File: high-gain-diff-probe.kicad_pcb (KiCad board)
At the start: 4 copper layers, 120 x 74.5 mm, 104 parts, among them J1 30V DC IN, J2 BNC, J4 BNC, J5 BNC, SW1 DP3T, SW2 DP3T, SW3 SPDT, SW4 DP3T, SW5 DP3T, SW6 SPDT, SW7 DP3T, U1 AD8428BRZ, U2 OP1177, U3 BUF634A, U6 LM393, U7 AD8671, U8 BUF634A

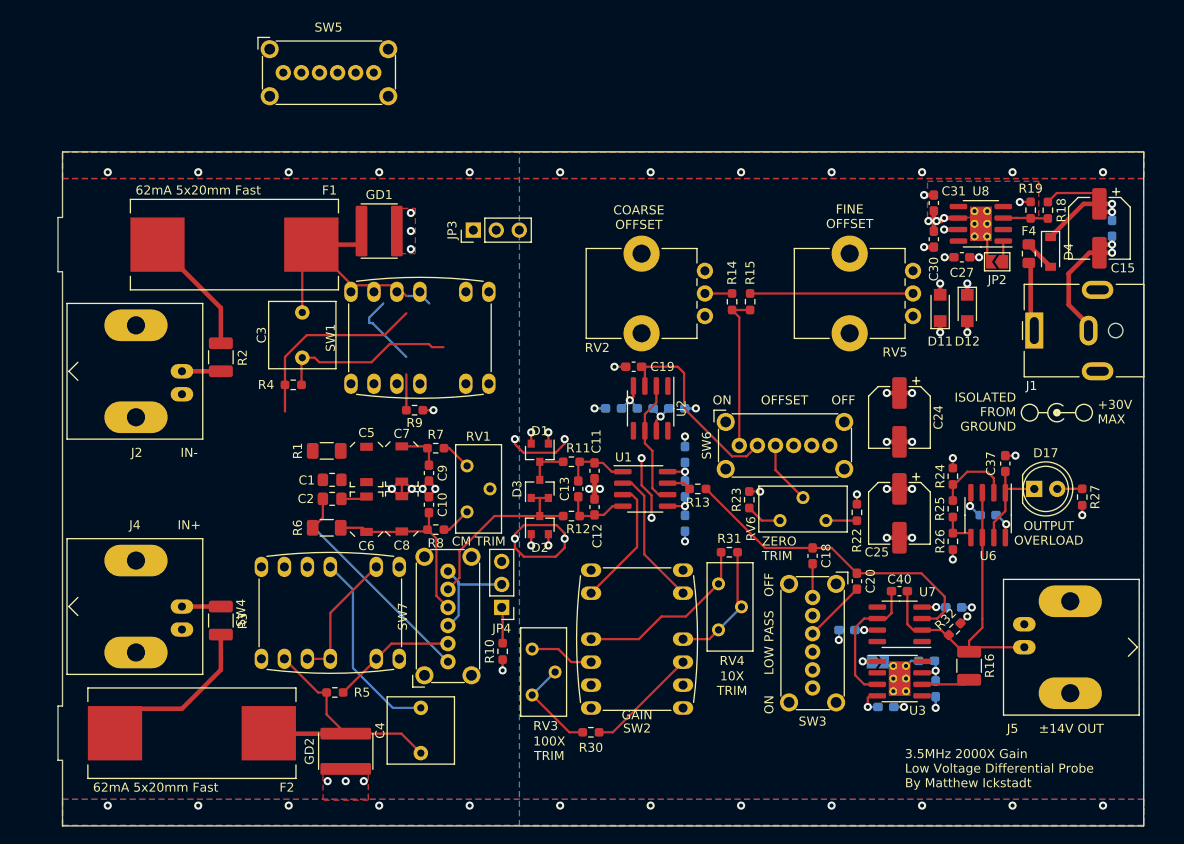
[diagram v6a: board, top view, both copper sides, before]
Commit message: Complete major layout of no-relay design
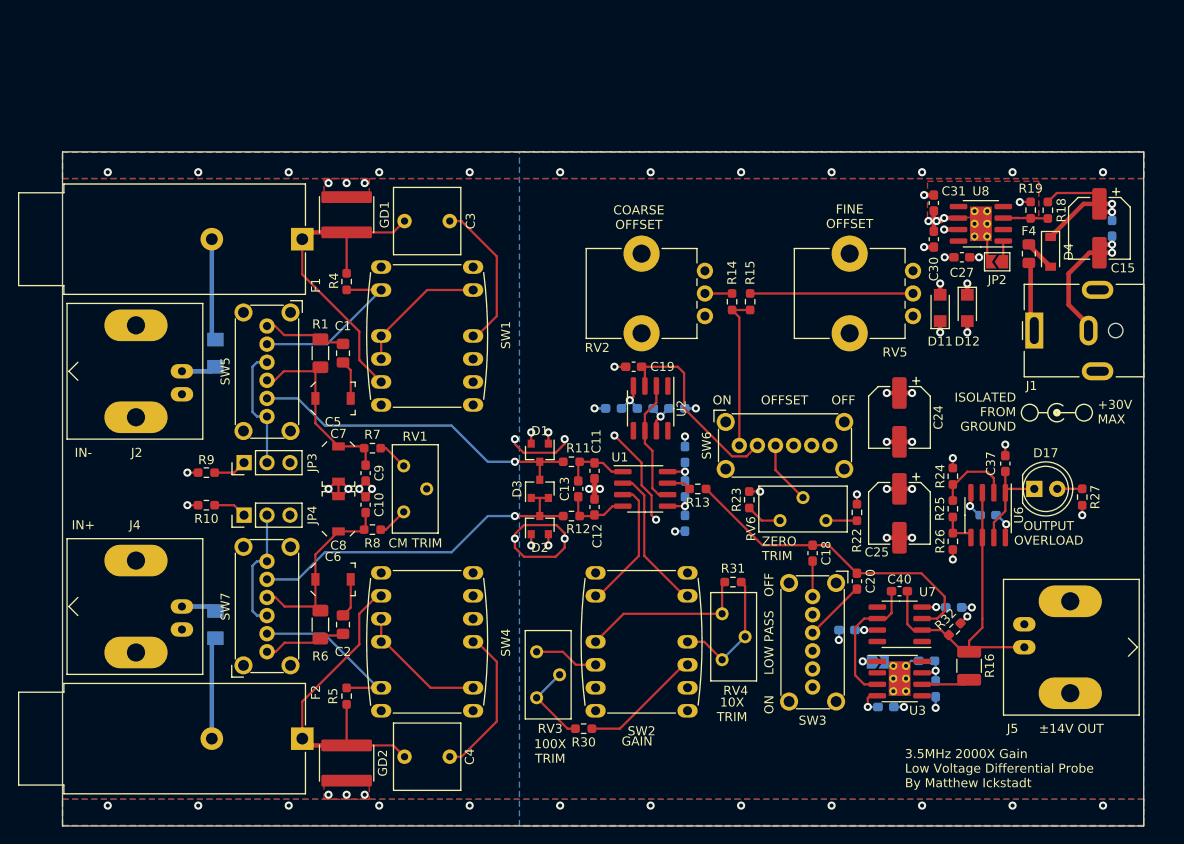
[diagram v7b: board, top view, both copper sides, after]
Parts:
- F1, F2: footprint high-gain-diff-probe:Fuseholder_Schurter_0031.8273 -> Fuse:Fuseholder_Cylinder-5x20mm_Schurter_FAB_0031-355x_Horizontal_Closed
- R2, R3: footprint Resistor_SMD:R_1210_3225Metric_Pad1.30x2.65mm_HandSolder -> Resistor_SMD:R_MiniMELF_MMA-0204; moved to B.Cu
- moved R10 36.5 mm to (105.9, 101.8), turned to 0 degrees
- moved JP3 36.1 mm to (110.1, 97.1)
- moved JP4 30.3 mm to (110.1, 102.9), turned to 90 degrees
- moved SW5 28.1 mm to (112.6, 82.0), turned to 270 degrees
- moved R9 24.0 mm to (105.9, 98.2), turned to 180 degrees
- moved C3 22.2 mm to (132.8, 70.4), turned to 180 degrees
- moved SW7 20.0 mm to (112.6, 118.0)
- moved C1 14.1 mm to (121.0, 85.0), turned to 90 degrees
- moved C2 14.0 mm to (121.0, 115.0), turned to 270 degrees
- moved R4 12.8 mm to (121.4, 77.1), turned to 270 degrees
- moved F2 12.2 mm to (116.5, 127.6)
- moved SW4 11.2 mm to (130.3, 116.9), turned to 270 degrees
- moved R1 10.8 mm to (118.5, 85.0), turned to 90 degrees
- moved R6 10.7 mm to (118.5, 115.0), turned to 270 degrees
- moved C5 8.18 mm to (119.9, 90.0), turned to 0 degrees
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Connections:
- R9 pad 1: Net-(JP3-Pad2) -> Net-(JP3-Pad1)
- SW1 pad 1: (no net) -> Net-(C3-Pad2)
- SW1 pad 2: GND -> Net-(SW1-Pad2)
- SW1 pad 3: Net-(C3-Pad1) -> Net-(SW1-Pad2)
- SW1 pad 4: Net-(C3-Pad2) -> (no net)
- SW1 pad 5: Net-(SW1-Pad5) -> GND
- SW1 pad 6: Net-(SW1-Pad5) -> Net-(C3-Pad1)
- SW1 pad C1: Net-(SW1-Pad5) -> Net-(R4-Pad2)
- SW1 pad C2: Net-(R4-Pad2) -> Net-(SW1-Pad2)
- SW5 pad 3: Net-(JP3-Pad1) -> Net-(JP3-Pad2)
- SW5 pad 6: Net-(JP3-Pad1) -> Net-(JP3-Pad2)
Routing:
- net /ATTEN-: track 4.59 -> 37.6 mm, vias 0 -> 1
- net /ATTEN+: track 21.7 -> 39.5 mm, vias 0 -> 1
- net Net-(C5-Pad1): track 4.86 -> 21.4 mm
- net (no net): track 15.7 -> 0.00 mm, vias 2 -> 0
- net Net-(C2-Pad2): track 24.4 -> 9.22 mm
- net Net-(SW1-Pad2): track 0.00 -> 14.8 mm
- net Net-(JP3-Pad2): track 3.98 -> 13.7 mm
- net Net-(C3-Pad2): track 26.3 -> 36.0 mm
- net GND: track 98.8 -> 89.5 mm, vias 61 -> 63
- net Net-(C1-Pad2): track 0.00 -> 9.22 mm
- net Net-(SW1-Pad1): track 8.47 -> 0.00 mm
- net Net-(F2-Pad2): track 18.5 -> 11.4 mm
- net Net-(C4-Pad2): track 29.3 -> 36.3 mm
- net Net-(C3-Pad1): track 22.7 -> 16.9 mm
- net Net-(R5-Pad2): track 13.9 -> 18.9 mm
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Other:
- board size 120 x 74.5 mm -> 119.5 x 74.5 mm

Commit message: Layout Tweaks
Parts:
- SW5, SW7: value DP3T -> DPDT
- moved D17 101.4 mm to (96.0, 101.3), turned to 90 degrees
- moved R27 67.9 mm to (142.9, 68.8), turned to 0 degrees
- moved D11 2.83 mm to (188.9, 82.1)
- moved D12 2.83 mm to (191.9, 82.1)
- moved C32 2.19 mm to (188.1, 111.0), turned to 270 degrees
- moved R32 1.73 mm to (190.3, 115.2), turned to 90 degrees
- moved C20 1.60 mm to (179.4, 110.1)
- moved C18 1.60 mm to (174.5, 107.1)
- moved SW3 1.60 mm to (174.5, 111.9)
- moved C21 1.55 mm to (187.1, 119.0)
- moved C29 1.55 mm to (178.2, 115.6)
- moved C33 1.55 mm to (188.1, 122.1)
- moved C35 1.55 mm to (182.6, 124.1)
- moved C40 1.55 mm to (184.1, 111.3)
- moved JP1 1.55 mm to (181.7, 119.1)
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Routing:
- net GND: track 89.5 -> 253.2 mm
- net Net-(C37-Pad2): track 11.4 -> 168.1 mm, vias 0 -> 1
- net Net-(D17-Pad2): track 2.77 -> 80.3 mm, vias 0 -> 1
- net /OUT: track 36.4 -> 34.6 mm
- net Net-(C18-Pad1): track 35.7 -> 37.4 mm
- net Net-(R14-Pad1): track 17.3 -> 16.6 mm
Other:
- board text added: "1M Term ON OFF"
